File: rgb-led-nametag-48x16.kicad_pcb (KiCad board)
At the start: 4 copper layers, 84 x 28.8 mm, 96 parts, among them J1 USB_C_Receptacle_USB2.0, Q1 CJ3139K, Q10 CJ3139K, Q11 CJ3139K, Q12 CJ3139K, Q13 CJ3139K, Q14 CJ3139K, Q15 CJ3139K, Q16 CJ3139K, Q2 CJ3139K, Q3 CJ3139K, Q4 CJ3139K, Q5 CJ3139K, Q6 CJ3139K, Q7 CJ3139K, Q8 CJ3139K, Q9 CJ3139K, U1 led-panel-16x16, U10 74HC595, U11 74HC595, U12 74HC595, U13 74HC595, U14 74HC595, U15 74HC595, U16 led-panel-16x16, U17 74HC595, U18 74HC595, U19 74HC595, U2 74HC595, U20 74HC595, U21 74HC595, U22 74HC595, U23 74HC595, U3 74HC595, U4 74HC595, U5 74HC595, U6 74HC595, U7 74HC595, U8 74HC595, U9 led-panel-16x16

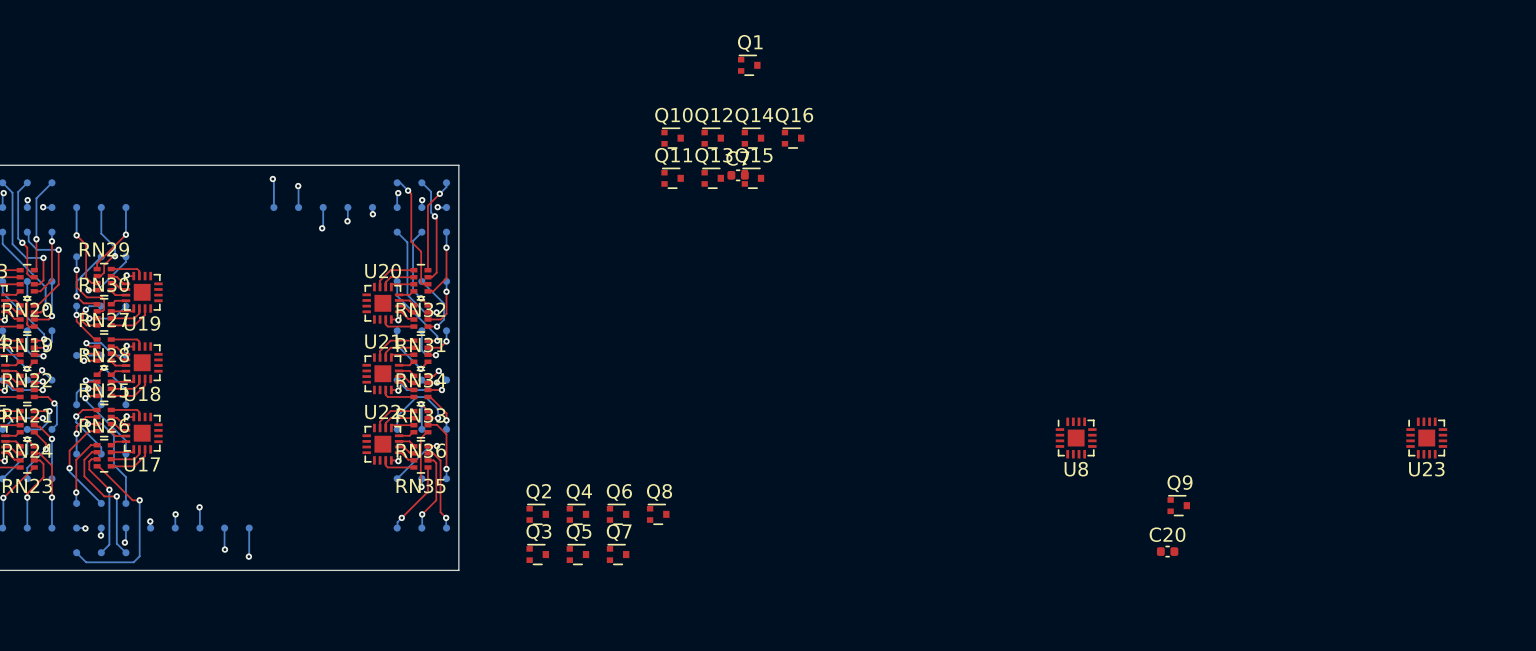
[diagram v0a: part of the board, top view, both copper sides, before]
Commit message: Finish anode driver 1-8 layout
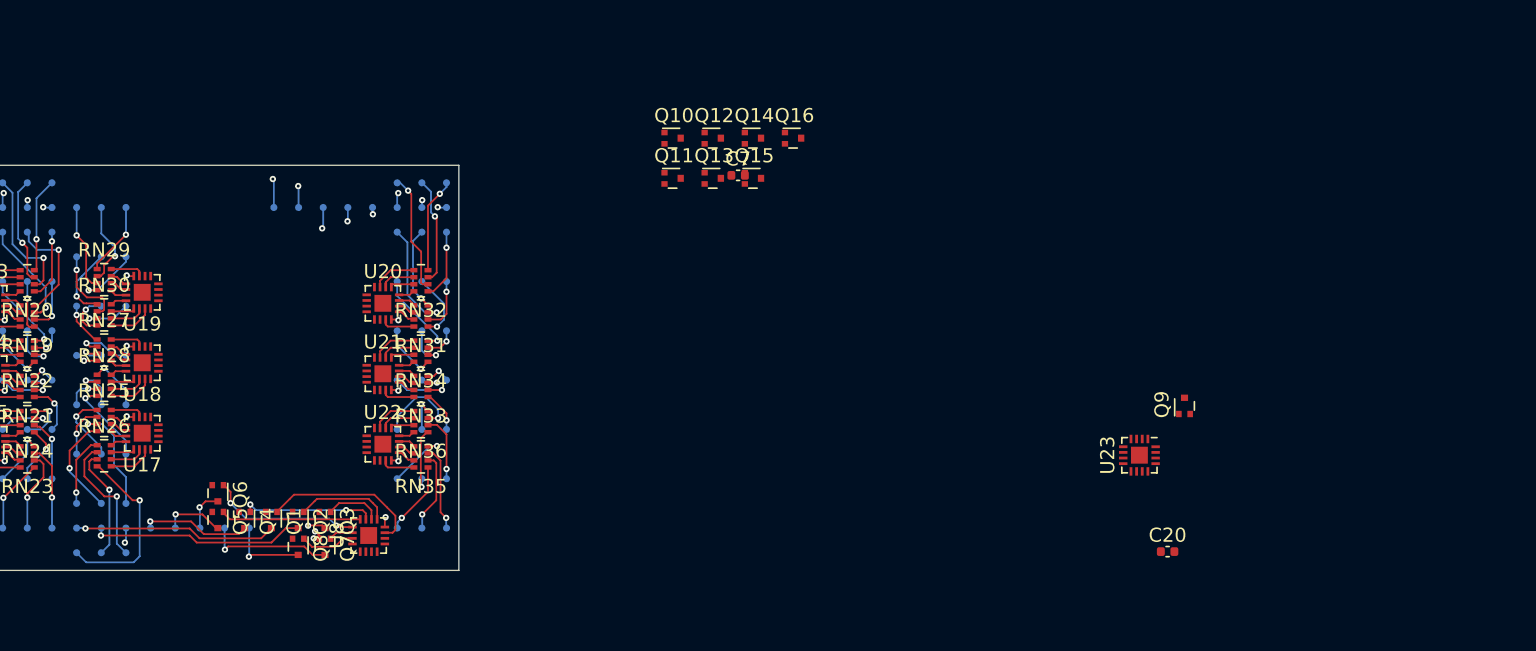
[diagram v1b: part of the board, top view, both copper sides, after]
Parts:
- moved U8 50.7 mm to (169.0, 121.0), turned to 270 degrees
- moved Q1 46.8 mm to (162.1, 119.9), turned to 270 degrees
- moved Q6 28.4 mm to (158.3, 118.0), turned to 270 degrees
- moved Q5 25.7 mm to (158.3, 119.9), turned to 270 degrees
- moved Q8 25.7 mm to (164.0, 121.8), turned to 270 degrees
- moved Q4 23.7 mm to (160.2, 119.9), turned to 270 degrees
- moved Q7 20.8 mm to (165.9, 121.8), turned to 270 degrees
- moved U23 20.4 mm to (223.7, 115.3), turned to 270 degrees
- moved Q2 17.0 mm to (164.0, 119.9), turned to 270 degrees
- moved Q3 15.3 mm to (165.9, 119.9), turned to 270 degrees
- moved Q9 7.09 mm to (226.9, 111.8), turned to 90 degrees
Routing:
- net /A3: track 59.2 -> 74.2 mm, vias 3 -> 4
- net /A2: track 57.6 -> 72.3 mm
- net /A1: track 57.9 -> 71.7 mm
- net Net-(Q1-Pad1): track 0.00 -> 11.4 mm
- net Net-(Q6-Pad1): track 0.00 -> 10.9 mm, vias 0 -> 2
- net Net-(Q5-Pad1): track 0.00 -> 9.99 mm
- net Net-(Q4-Pad1): track 0.00 -> 9.39 mm, vias 0 -> 2
- net /A7: track 60.6 -> 68.1 mm
- net /A4: track 57.7 -> 65.0 mm
- net Net-(Q2-Pad1): track 0.00 -> 6.63 mm
- net Net-(Q3-Pad1): track 0.00 -> 4.01 mm
- net Net-(Q8-Pad1): track 0.00 -> 3.99 mm
- net /A8: track 62.0 -> 65.6 mm
- net /A5: track 59.2 -> 62.6 mm
- net VBUS: track 9.37 -> 11.1 mm, vias 18 -> 21
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
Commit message: Add driver bypassing
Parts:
- moved C6 221.2 mm to (170.8, 111.8)
- moved C9 220.6 mm to (170.7, 118.5), turned to 315 degrees
- moved C17 218.0 mm to (173.6, 122.1)
- moved C8 213.3 mm to (170.8, 106.8)
- moved C4 203.1 mm to (163.4, 103.5), turned to 90 degrees
- moved C5 202.4 mm to (151.9, 101.0), turned to 315 degrees
- moved C10 201.1 mm to (152.2, 111.5), turned to 180 degrees
- moved C14 200.0 mm to (152.2, 106.4), turned to 180 degrees
- moved C12 199.9 mm to (123.9, 111.5), turned to 180 degrees
- moved C15 197.6 mm to (142.4, 101.5), turned to 45 degrees
- moved C13 196.8 mm to (142.9, 111.8)
- moved C11 196.7 mm to (142.8, 106.8)
- moved C16 189.1 mm to (123.9, 106.5), turned to 180 degrees
- moved C18 179.2 mm to (123.8, 101.0), turned to 315 degrees
- moved C19 172.3 mm to (114.9, 106.8)
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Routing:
- net GND: track 0.00 -> 34.2 mm, vias 0 -> 21
- net /Panel 1/sheet61A6C351/SIN: track 0.00 -> 30.3 mm, vias 0 -> 2
- net /sheet61C56D2D/SIN: track 0.00 -> 27.4 mm, vias 0 -> 2
- net /Panel 2/sheet61A6C351/SIN: track 0.00 -> 23.1 mm, vias 0 -> 2
- net VBUS: track 11.1 -> 34.0 mm, vias 21 -> 48
- net /Panel 3/sheet61A6C351/SIN: track 0.00 -> 19.0 mm, vias 0 -> 2
- net /A9: track 61.4 -> 71.5 mm
- net /A10: track 60.6 -> 70.4 mm
- net /A11: track 60.7 -> 68.8 mm
- net Net-(Q9-Pad1): track 0.00 -> 6.91 mm
- net Net-(Q16-Pad1): track 0.00 -> 6.60 mm
- net Net-(Q15-Pad1): track 0.00 -> 4.63 mm
- net Net-(Q10-Pad1): track 0.00 -> 4.42 mm
- net /Panel 1/sheet61A68DA0/SIN: track 0.00 -> 3.69 mm
- net /Panel 1/Sheet61A5C766/SIN: track 0.00 -> 3.69 mm
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
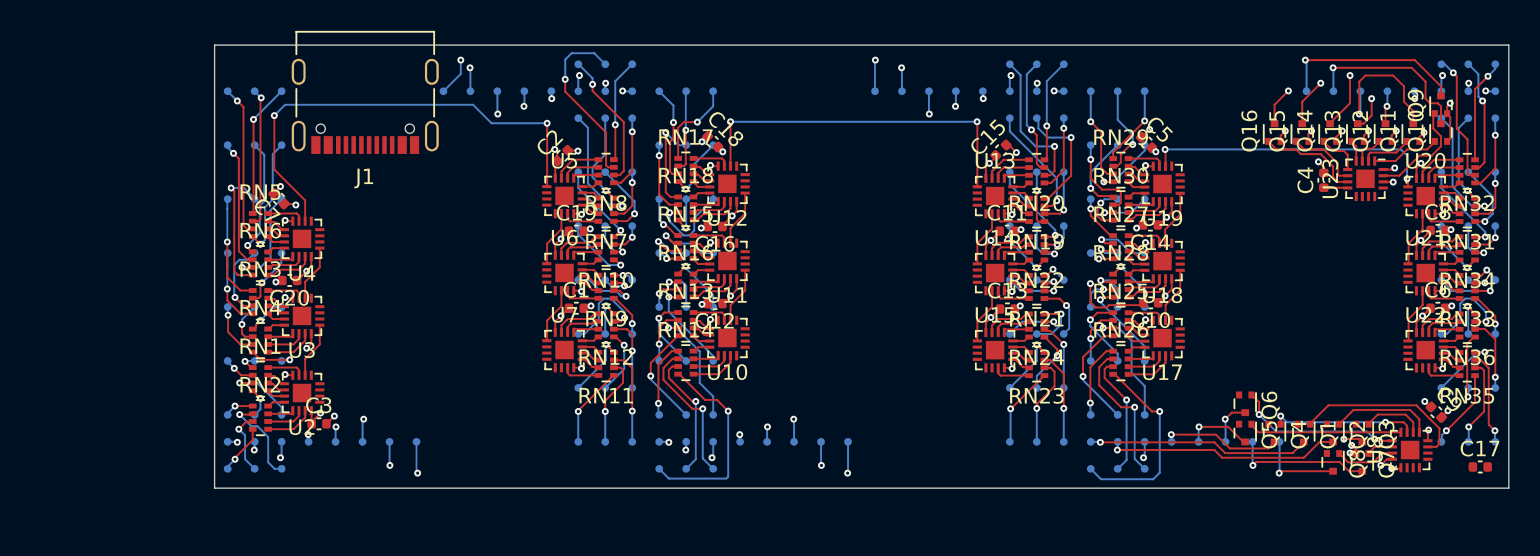
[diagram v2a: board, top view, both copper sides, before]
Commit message: Finish STM32 digital interface assignment
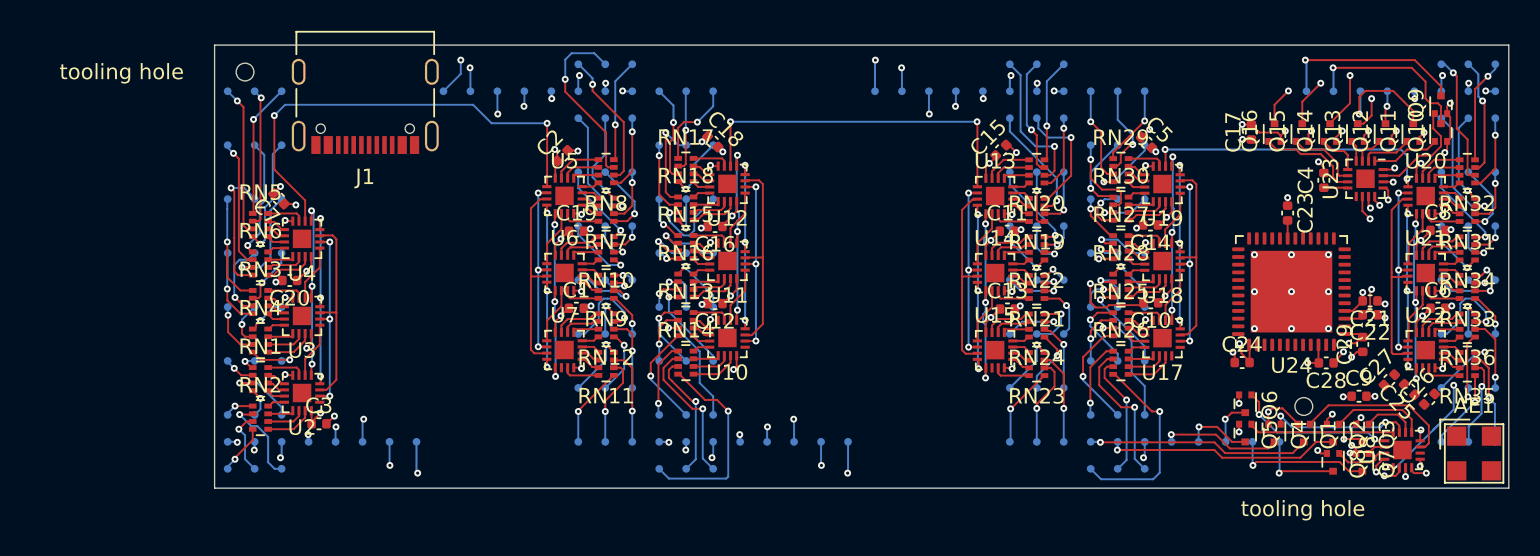
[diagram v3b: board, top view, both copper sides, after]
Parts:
- added AE1: Antenna, Antenna_SMD_Molex:2065130001, F.Cu at (173.2, 121.2)
- added C21: 10uF, Capacitor_SMD:C_0402_1005Metric, F.Cu at (166.4, 111.3)
- added C22: 10uF, Capacitor_SMD:C_0402_1005Metric, F.Cu at (166.4, 112.2)
- added C23: 10uF, Capacitor_SMD:C_0402_1005Metric, F.Cu at (161.1, 105.6)
- added C24: 10uF, Capacitor_SMD:C_0402_1005Metric, F.Cu at (158.1, 115.3)
- added C25: 0R, Capacitor_SMD:C_0402_1005Metric, F.Cu at (168.9, 117.1)
- added C26: DNP, Capacitor_SMD:C_0402_1005Metric, F.Cu at (170.2, 117.7)
- added C27: DNP, Capacitor_SMD:C_0402_1005Metric, F.Cu at (167.7, 116.5)
- added C28: 10uF, Capacitor_SMD:C_0402_1005Metric, F.Cu at (163.6, 115.3)
- added C29: 10uF, Capacitor_SMD:C_0402_1005Metric, F.Cu at (165.9, 114.2)
- added H1: ToolingHole, ToolingHole:ToolingHole_JLCSMT, F.Cu at (162.1, 118.2)
- added H2: ToolingHole, ToolingHole:ToolingHole_JLCSMT, F.Cu at (93.4, 96.5)
- added U24: ESP32-PICO-D4, Package_DFN_QFN:QFN-48-1EP_7x7mm_P0.5mm_EP5.3x5.3mm, F.Cu at (161.3, 110.7)
- moved C17 26.3 mm to (158.7, 100.4), turned to 90 degrees
- moved C9 5.12 mm to (165.7, 117.5), turned to 0 degrees
- moved U8 0.50 mm to (168.5, 121.0)
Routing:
- net /Panel 2/CLK_LOW: track 0.00 -> 25.5 mm
- net /Panel 3/CLK_LOW: track 0.00 -> 25.5 mm
- net /Panel 1/CLK_LOW: track 0.00 -> 25.4 mm
- net /Low side 1/LATCH: track 0.00 -> 24.7 mm, vias 0 -> 2
- net /Panel 2/~OE~_LOW: track 0.00 -> 24.5 mm, vias 0 -> 6
- net /Panel 3/~OE~_LOW: track 0.00 -> 24.4 mm, vias 0 -> 6
- net /Panel 1/~OE~_LOW: track 0.00 -> 24.1 mm, vias 0 -> 6
- net /Panel 2/~RST~_LOW: track 0.00 -> 23.7 mm, vias 0 -> 6
- net /Panel 1/~RST~_LOW: track 0.00 -> 23.6 mm, vias 0 -> 6
- net /Panel 2/LATCH_LOW: track 0.00 -> 23.5 mm, vias 0 -> 6
- net /Panel 1/LATCH_LOW: track 0.00 -> 23.5 mm, vias 0 -> 6
- net /Panel 3/~RST~_LOW: track 0.00 -> 23.3 mm, vias 0 -> 6
- net /Panel 3/LATCH_LOW: track 0.00 -> 23.2 mm, vias 0 -> 6
- net /Low side 1/~OE: track 0.00 -> 22.8 mm, vias 0 -> 2
- net /Low side 1/~RST: track 0.00 -> 22.5 mm, vias 0 -> 2
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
